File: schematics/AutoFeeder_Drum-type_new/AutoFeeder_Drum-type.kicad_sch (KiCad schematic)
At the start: 45 parts, among them J1 USB_C_Receptacle_6, J2 Conn_01x04, J3 Conn_01x05, J4 Conn_02x02_Odd_Even, J5 Conn_01x04, J6 Conn_02x03_Odd_Even, J7 Conn_01x04, J8 Conn_01x03, J9 Conn_01x04, M1 Motor_DC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

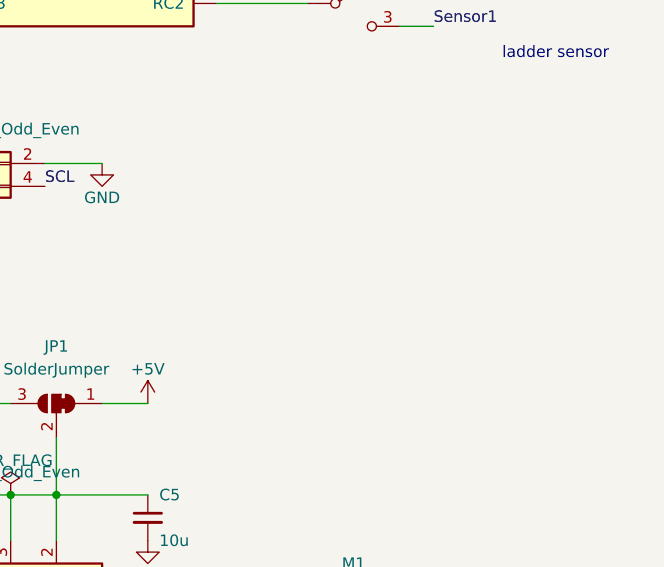
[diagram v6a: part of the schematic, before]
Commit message: An IOC interrupt was used to detect the falling edge of the CW switch; two timers Timer4/Timer6 were used to eliminate the chatter that occurs on the falling and rising edges of the CW switch. These interrupts made the AS5600 and LCD currently hanging on I2C unusable...
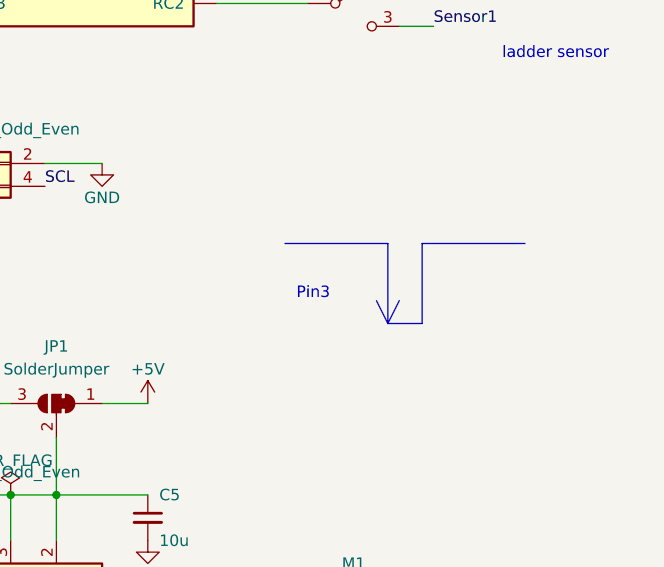
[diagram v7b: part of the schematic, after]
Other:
- note added: "Pin3"
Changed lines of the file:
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@@
     (stroke (width 0) (type default) (color 0 0 0 0))
+  )
+  (polyline (pts (xy 254 110.49) (xy 255.27 113.03))
+    (stroke (width 0) (type solid) (color 0 0 0 0))
   )
   (wire (pts (xy 198.12 67.31) (xy 205.74 67.31))
@@
     (stroke (width 0) (type solid) (color 0 0 0 0))
   )
+  (polyline (pts (xy 243.84 104.14) (xy 255.27 104.14))
+    (stroke (width 0) (type default) (color 0 0 0 0))
+  )
   (polyline (pts (xy 87.63 55.88) (xy 86.36 58.42))
     (stroke (width 0) (type solid) (color 0 0 255 1))
@@
     (stroke (width 0) (type default) (color 0 0 0 0))
   )
+  (polyline (pts (xy 255.27 104.14) (xy 255.27 113.03))
+    (stroke (width 0) (type solid) (color 0 0 0 0))
+  )
   (wire (pts (xy 135.89 29.21) (xy 148.59 29.21))
     (stroke (width 0) (type default) (color 0 0 0 0))
@@
     (stroke (width 0) (type default) (color 0 0 0 0))
   )
+  (polyline (pts (xy 259.08 113.03) (xy 259.08 104.14))
+    (stroke (width 0) (type default) (color 0 0 0 0))
+  )
   (wire (pts (xy 46.99 88.9) (xy 53.34 88.9))
     (stroke (width 0) (type default) (color 0 0 0 0))
@@
     (stroke (width 0) (type default) (color 0 0 0 0))
   )
+  (polyline (pts (xy 255.27 113.03) (xy 259.08 113.03))
+    (stroke (width 0) (type default) (color 0 0 0 0))
+  )
   (polyline (pts (xy 170.18 97.79) (xy 170.18 143.51))
     (stroke (width 0) (type default) (color 0 0 0 0))
@@
     (stroke (width 0) (type default) (color 0 0 0 0))
   )
+  (polyline (pts (xy 259.08 104.14) (xy 270.51 104.14))
+    (stroke (width 0) (type default) (color 0 0 0 0))
+  )
   (wire (pts (xy 201.93 53.34) (xy 201.93 54.61))
     (stroke (width 0) (type default) (color 0 0 0 0))
@@
     (stroke (width 0) (type default) (color 0 0 0 0))
   )
+  (polyline (pts (xy 255.27 113.03) (xy 256.54 110.49))
+    (stroke (width 0) (type solid) (color 0 0 0 0))
+  )
   (wire (pts (xy 187.96 69.85) (xy 187.96 71.12))
     (stroke (width 0) (type default) (color 0 0 0 0))
@@
     (stroke (width 0) (type solid) (color 0 0 0 0))
   )
+  (text "Pin3" (at 245.11 110.49 0)
+    (effects (font (size 1.27 1.27)) (justify left bottom))
+  )
   (text "Green" (at 260.35 55.88 0)
